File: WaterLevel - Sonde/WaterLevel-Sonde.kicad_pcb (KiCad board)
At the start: 2 copper layers, 46.2 x 43.2 mm, 16 parts, among them P1 12V, P2 VOUT, P3 GND, P4 PGND, P5 PHOT, U1 LM741, U2 LM555N, U3 LM555N

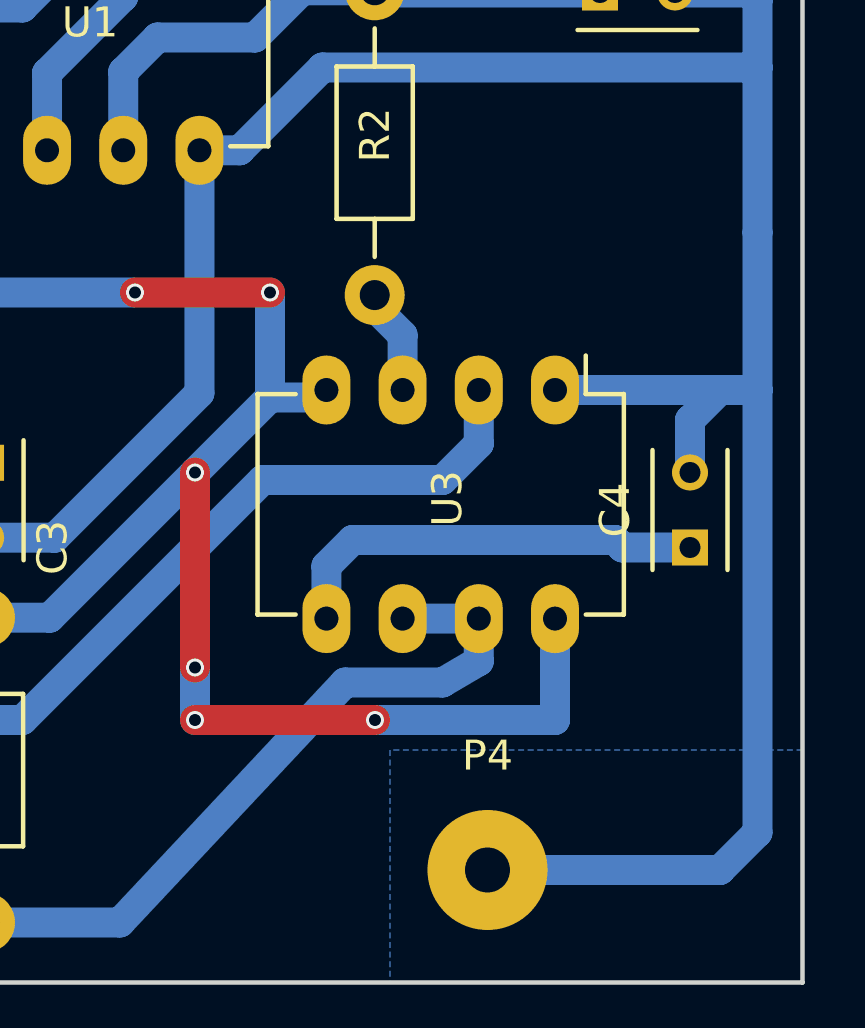
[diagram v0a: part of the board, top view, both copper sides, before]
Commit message: Fixed Sonde Before display test
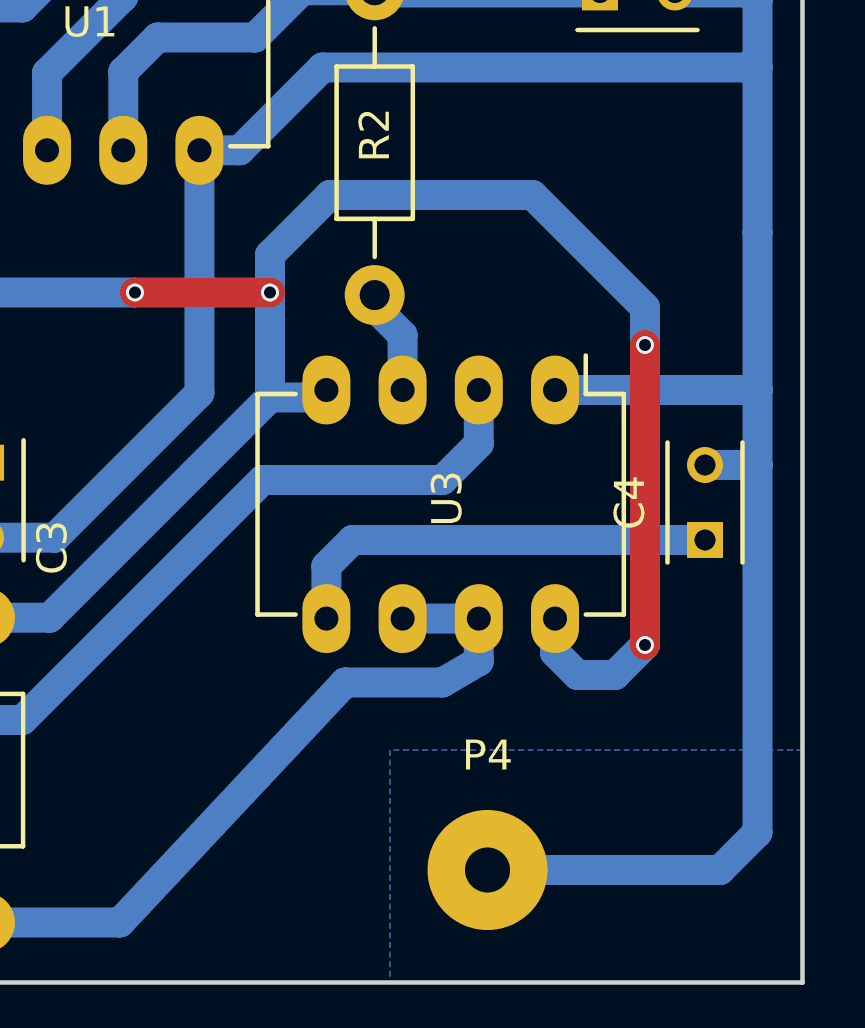
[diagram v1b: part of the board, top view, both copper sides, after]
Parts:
- moved C4 0.56 mm to (183.2, 104.8)
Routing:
- net +12V: track 114.9 -> 123.8 mm, vias 6 -> 4
- net GND: track 115.1 -> 114.2 mm
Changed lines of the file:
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@@
     (links 31)
     (no_connects 0)
-    (area 140.174999 76.174999 186.575001 119.575001)
+    (area 140.174999 75.156047 186.575001 119.575001)
     (thickness 1.6)
     (drawings 4)
-    (tracks 121)
+    (tracks 126)
     (zones 0)
     (modules 16)
@@
     (pad_to_mask_clearance 0.2)
     (aux_axis_origin 0 0)
+    (grid_origin 140.25 76.25)
     (visible_elements FFFFFF7F)
     (pcbplotparams
@@
   )
   (module Capacitors_ThroughHole:C_Rect_L4_W2.5_P2.5 (layer F.Cu)
-    (at 182.75 105 90)
+    (at 183.25 104.75 90)
     (descr "Film Capacitor Length 4mm x Width 2.5mm, Pitch 2.5mm")
     (tags Capacitor)
@@
   (segment (start 165 88) (end 163.858 89.142) (width 1) (layer B.Cu) (net 1))
   (segment (start 163.858 89.142) (end 163.858 91.76) (width 1) (layer B.Cu) (net 1))
+  (segment (start 183.25 102.25) (end 185 102.25) (width 1) (layer B.Cu) (net 2) (status 400000))
+  (segment (start 185 102.25) (end 184.75 102.25) (width 1) (layer B.Cu) (net 2))
+  (segment (start 184.75 102.25) (end 185 102.25) (width 1) (layer B.Cu) (net 2))
   (segment (start 143.25 106.25) (end 146.75 106.25) (width 1) (layer B.Cu) (net 2))
   (segment (start 146.75 106.25) (end 147.25 106.75) (width 1) (layer B.Cu) (net 2))
-  (segment (start 182.75 102.5) (end 182.75 100.75) (width 1) (layer B.Cu) (net 2))
-  (segment (start 182.75 100.75) (end 183.75 99.75) (width 1) (layer B.Cu) (net 2))
   (segment (start 147.25 108.5) (end 147.25 106.75) (width 1) (layer B.Cu) (net 2))
   (segment (start 149.326 104.674) (end 159.286 104.674) (width 1) (layer B.Cu) (net 2))
@@
   (segment (start 185 89) (end 185 94.5) (width 1) (layer B.Cu) (net 2))
   (segment (start 185 94.5) (end 185 99.75) (width 1) (layer B.Cu) (net 2))
-  (segment (start 185 99.75) (end 185 114.5) (width 1) (layer B.Cu) (net 2))
+  (segment (start 185 99.75) (end 185 102.25) (width 1) (layer B.Cu) (net 2))
+  (segment (start 185 102.25) (end 185 114.5) (width 1) (layer B.Cu) (net 2))
   (segment (start 182.908 80.076) (end 182.908 81.158) (width 1) (layer B.Cu) (net 2))
   (segment (start 149.79 108.5) (end 149.79 110.21) (width 1) (layer B.Cu) (net 3))
@@
   (segment (start 154.87 100.88) (end 157.992 100.88) (width 1) (layer B.Cu) (net 4))
   (segment (start 157.992 100.88) (end 159.286 102.174) (width 1) (layer B.Cu) (net 4))
-  (segment (start 182.75 105) (end 180.5 105) (width 1) (layer B.Cu) (net 5))
+  (segment (start 183.25 104.75) (end 180.25 104.75) (width 1) (layer B.Cu) (net 5) (status 400000))
+  (segment (start 180.25 104.75) (end 171.5 104.75) (width 1) (layer B.Cu) (net 5))
+  (segment (start 171.5 104.75) (end 170.63 105.62) (width 1) (layer B.Cu) (net 5))
   (segment (start 170.63 105.62) (end 170.63 107.37) (width 1) (layer B.Cu) (net 5))
-  (segment (start 171.5 104.75) (end 170.63 105.62) (width 1) (layer B.Cu) (net 5))
-  (segment (start 180.25 104.75) (end 171.5 104.75) (width 1) (layer B.Cu) (net 5))
-  (segment (start 180.5 105) (end 180.25 104.75) (width 1) (layer B.Cu) (net 5))
-  (segment (start 178.25 107.37) (end 178.25 110.75) (width 1) (layer B.Cu) (net 6))
-  (via (at 166.25 102.5) (size 0.6) (drill 0.4) (layers F.Cu B.Cu) (net 6))
-  (segment (start 166.25 109) (end 166.25 102.5) (width 1) (layer F.Cu) (net 6))
-  (via (at 166.25 109) (size 0.6) (drill 0.4) (layers F.Cu B.Cu) (net 6))
-  (segment (start 166.25 110.75) (end 166.25 109) (width 1) (layer B.Cu) (net 6))
-  (via (at 166.25 110.75) (size 0.6) (drill 0.4) (layers F.Cu B.Cu) (net 6))
-  (segment (start 172.25 110.75) (end 166.25 110.75) (width 1) (layer F.Cu) (net 6))
-  (via (at 172.25 110.75) (size 0.6) (drill 0.4) (layers F.Cu B.Cu) (net 6))
-  (segment (start 178.25 110.75) (end 172.25 110.75) (width 1) (layer B.Cu) (net 6))
+  (segment (start 181.25 97) (end 181.25 98.25) (width 1) (layer B.Cu) (net 6))
+  (segment (start 168.75 95.25) (end 170.75 93.25) (width 1) (layer B.Cu) (net 6))
+  (segment (start 170.75 93.25) (end 177.5 93.25) (width 1) (layer B.Cu) (net 6))
+  (segment (start 177.5 93.25) (end 181.25 97) (width 1) (layer B.Cu) (net 6))
+  (segment (start 168.75 96.5) (end 168.75 95.25) (width 1) (layer B.Cu) (net 6))
+  (segment (start 179 109.25) (end 178.25 108.5) (width 1) (layer B.Cu) (net 6) (status 800000))
+  (segment (start 180.25 109.25) (end 179 109.25) (width 1) (layer B.Cu) (net 6))
+  (segment (start 181.25 108.25) (end 180.25 109.25) (width 1) (layer B.Cu) (net 6))
+  (via (at 181.25 108.25) (size 0.6) (drill 0.4) (layers F.Cu B.Cu) (net 6))
+  (segment (start 181.25 98.25) (end 181.25 108.25) (width 1) (layer F.Cu) (net 6))
+  (via (at 181.25 98.25) (size 0.6) (drill 0.4) (layers F.Cu B.Cu) (net 6))
+  (segment (start 178.25 108.5) (end 178.25 107.37) (width 1) (layer B.Cu) (net 6) (status C00000))
+  (segment (start 168.75 100) (end 170.38 100) (width 1) (layer B.Cu) (net 6) (status 800000))
+  (segment (start 170.38 100) (end 170.63 99.75) (width 1) (layer B.Cu) (net 6) (status C00000))
   (segment (start 156.75 87) (end 156.75 87.25) (width 1) (layer B.Cu) (net 6))
   (segment (start 168.75 96.5) (end 168.75 100) (width 1) (layer B.Cu) (net 6))
@@
   (segment (start 161.41 107.34) (end 166.25 102.5) (width 1) (layer B.Cu) (net 6))
   (segment (start 166.25 102.5) (end 168.75 100) (width 1) (layer B.Cu) (net 6))
-  (segment (start 168.75 100) (end 170.38 100) (width 1) (layer B.Cu) (net 6))
   (segment (start 170.38 100) (end 170.63 99.75) (width 1) (layer B.Cu) (net 6))
   (segment (start 154.87 108.5) (end 158.09 108.5) (width 1) (layer B.Cu) (net 6))

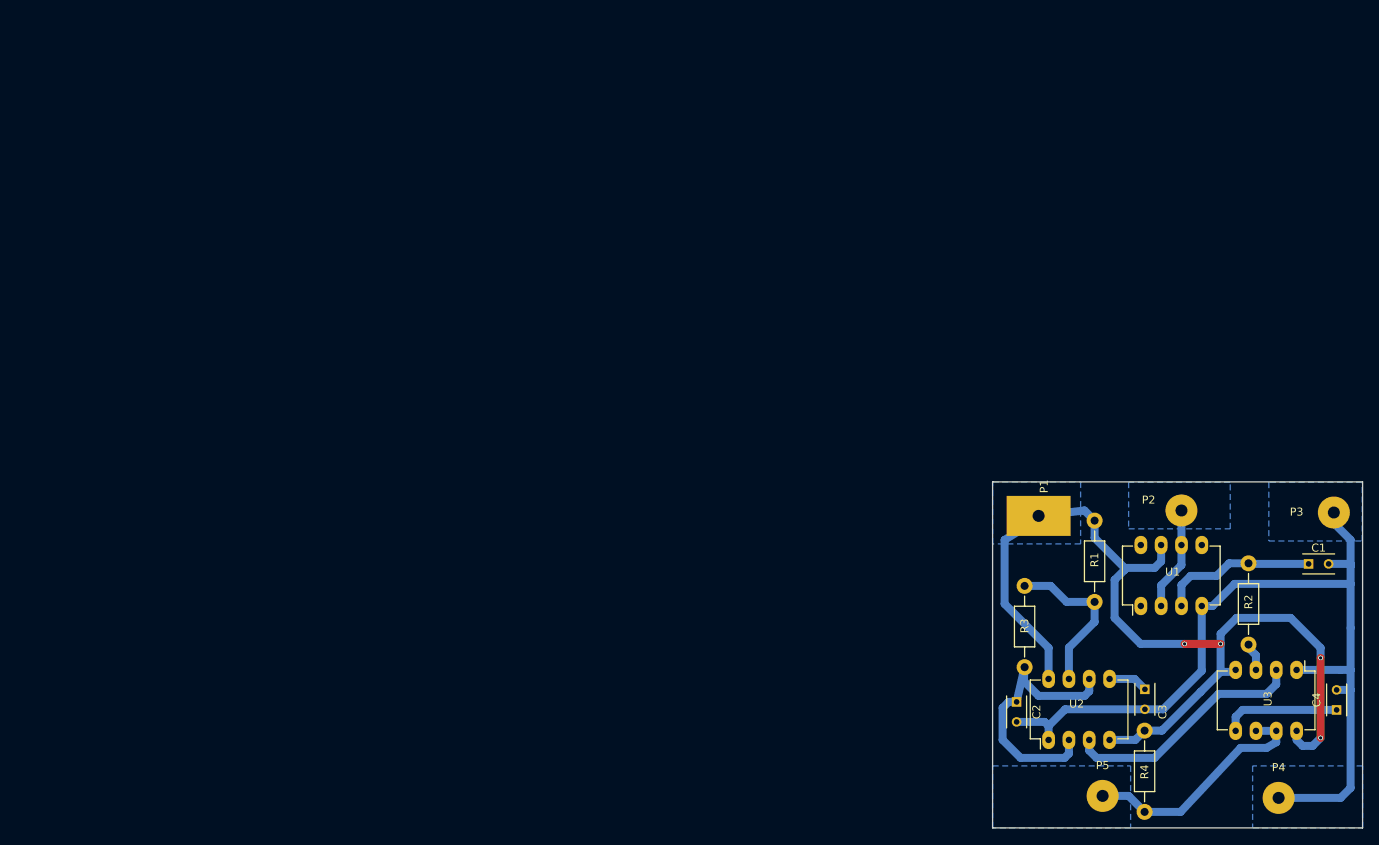
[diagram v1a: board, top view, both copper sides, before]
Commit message: Fixed a few issues with the probe, added copyright.
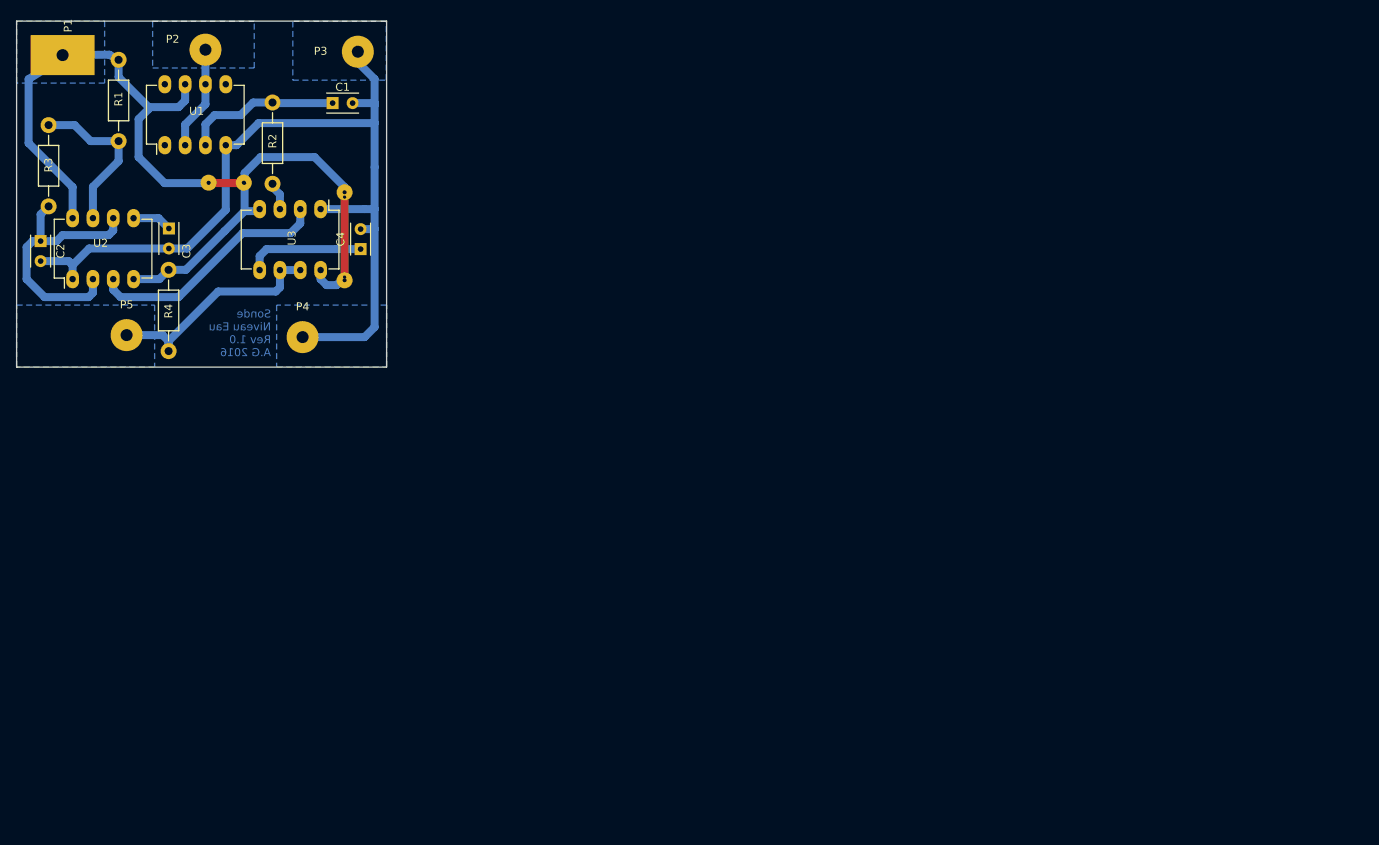
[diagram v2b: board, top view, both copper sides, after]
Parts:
- added via11: via, Wire_Pads:Big_Square_Pad_3mm_1mmDrill, F.Cu at (42.2, 38.9)
- added via12: via, Wire_Pads:Big_Square_Pad_3mm_1mmDrill, F.Cu at (46.6, 38.9)
- added via13: via, Wire_Pads:Big_Square_Pad_3mm_1mmDrill, F.Cu at (59.2, 40.0)
- added via14: via, Wire_Pads:Big_Square_Pad_3mm_1mmDrill, F.Cu at (59.2, 51.0)
- moved C1 134.9 mm to (57.8, 28.9)
- moved C2 134.9 mm to (21.2, 46.1)
- moved C3 134.9 mm to (37.3, 44.6)
- moved C4 134.9 mm to (61.2, 47.1)
- moved P1 134.9 mm to (24.0, 22.9)
- moved P2 134.9 mm to (41.9, 22.2)
- moved P4 134.9 mm to (54.0, 58.1)
- moved P5 134.9 mm to (32.0, 57.9)
- moved R1 134.9 mm to (31.0, 33.6)
- moved R2 134.9 mm to (50.2, 39.0)
- moved R3 134.9 mm to (22.2, 31.6)
- moved R4 134.9 mm to (37.2, 59.9)
- moved U1 134.9 mm to (36.8, 34.2)
- moved U2 134.9 mm to (25.2, 50.9)
- moved U3 134.9 mm to (56.2, 42.1)
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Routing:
- net Net-(C2-Pad1): track 34.1 -> 33.1 mm
- net Net-(P5-Pad1): track 30.2 -> 29.5 mm
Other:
- board text added: "Sonde Niveau Eau Rev 1.0 A.G 2016"
